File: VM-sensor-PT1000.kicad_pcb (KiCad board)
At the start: 2 copper layers, 26 x 24.8 mm, 20 parts, among them P1 PT100, P2 ADC, P3 PWR, U1 AMS1117, U2 MCP6001

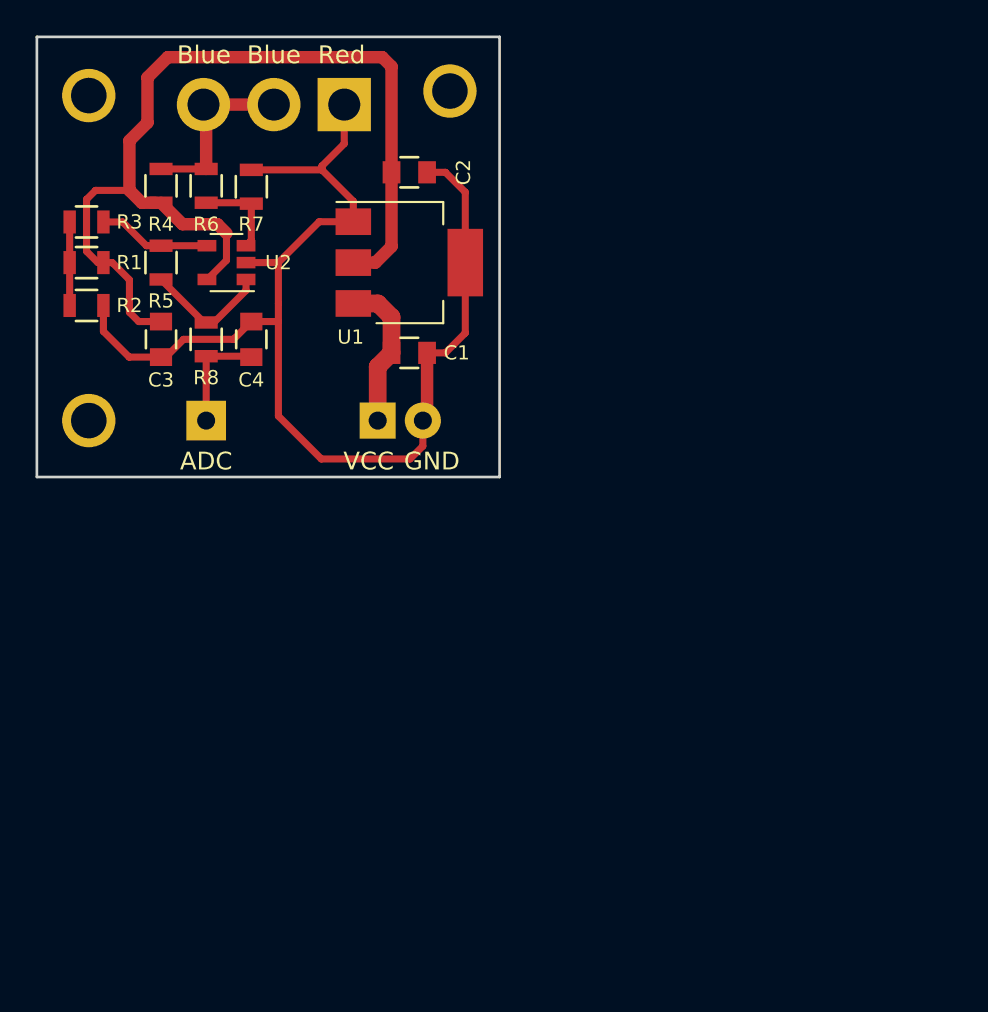
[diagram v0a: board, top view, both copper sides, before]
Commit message: add led PWR & change header ADC
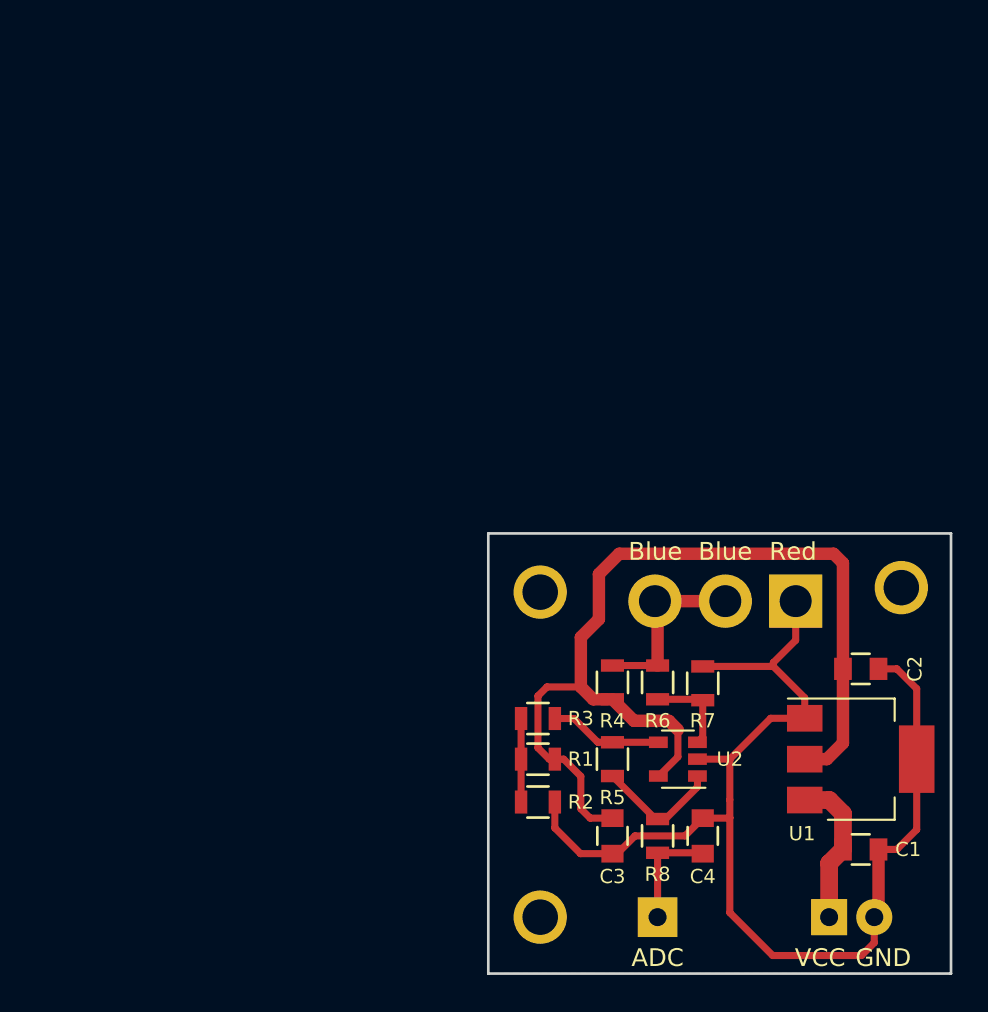
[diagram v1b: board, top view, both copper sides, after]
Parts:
- moved C1 37.8 mm to (160.0, 105.4)
- moved C2 37.8 mm to (160.0, 95.2)
- moved C3 37.8 mm to (146.1, 104.6)
- moved P1 37.8 mm to (156.4, 91.4)
- moved P2 37.8 mm to (148.6, 109.2)
- moved R1 37.8 mm to (141.9, 100.3)
- moved R2 37.8 mm to (141.9, 102.7)
- moved R3 37.8 mm to (141.9, 98.0)
- moved R4 37.8 mm to (146.1, 96.0)
- moved R5 37.8 mm to (146.1, 100.3)
- moved R6 37.8 mm to (148.6, 96.0)
- moved R8 37.8 mm to (148.6, 104.6)
- moved REF** 37.8 mm to (142.0, 90.9)
- moved REF** 37.8 mm to (162.3, 90.7)
- moved U1 37.8 mm to (160.0, 100.3)
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
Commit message: completed new PCB design
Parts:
- removed P1: PT100, Connectors_Hirose:Hirose_DF63-3P-3.96DSA_03x3.96mm_Straight
- removed REF** (x3): SolderWirePad_single_1-2mmDrill, Wire_Pads:SolderWirePad_single_1-2mmDrill
- added D1: LED_Small, LEDs:LED-3MM, F.Cu at (123.8, 89.2)
- added PT100: PT100, lib:Domino-PT100.pretty, F.Cu at (151.6, 96.2)
- added R9: 100R/1%, Resistors_SMD:R_0805, F.Cu at (127.5, 90.8)
- C3: value lib:C_0603 -> 10uF
- P2: footprint Pin_Headers:Pin_Header_Straight_1x01 -> w_conn_jst-ph:s2b-ph-kl
- P3: footprint Pin_Headers:Pin_Header_Straight_1x02 -> w_conn_jst-ph:s2b-ph-kl
- R2: value 100/1% -> 100R/1%
- R3, R6: value 1K/1% -> 16.9K/1%
- R5, R7: value 100K/1% -> 1M/1%
- U2: value MCP6001 -> MCP601T
- moved P3 40.1 mm to (126.4, 84.8), turned to 270 degrees
- moved U1 29.0 mm to (135.2, 85.4), turned to 180 degrees
- moved C1 28.7 mm to (141.9, 83.1)
- moved P2 25.7 mm to (126.4, 96.2)
- moved C4 22.3 mm to (130.9, 95.3)
- moved C2 20.6 mm to (141.9, 85.4)
- moved R8 17.8 mm to (133.4, 95.3)
- moved C3 17.4 mm to (141.9, 87.7), turned to 0 degrees
- moved R7 14.4 mm to (137.0, 98.8), turned to 180 degrees
- moved U2 13.7 mm to (137.0, 95.3), turned to 0 degrees
- moved R2 12.7 mm to (141.9, 90.0), turned to 180 degrees
- moved R5 12.2 mm to (137.0, 92.2), turned to 180 degrees
- moved R6 6.72 mm to (141.9, 96.6), turned to 0 degrees
- moved R1 5.93 mm to (141.9, 94.4), turned to 0 degrees
- moved R3 5.84 mm to (141.9, 92.2), turned to 0 degrees
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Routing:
- net GND: track 68.1 -> 110.0 mm
- net +3V3: track 55.9 -> 34.5 mm
- net /Blue: track 10.2 -> 18.2 mm
- net VCC: track 8.61 -> 15.8 mm
- net Net-(D1-Pad2): track 0.00 -> 4.12 mm
- net Net-(R6-Pad1): track 5.05 -> 7.79 mm
- net Net-(R5-Pad2): track 7.27 -> 4.76 mm
- net Net-(R3-Pad1): track 6.38 -> 7.95 mm
- net /ADC: track 6.18 -> 7.50 mm
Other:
- board size 26 x 24.8 mm -> 40 x 21 mm
- net class Default: trace_width 0.7 -> 1
- board text added: "+"
- board text added: "-"
- board text added: "BLUE"
- board text added: "PWR"
- board text added: "RED"
- board text removed: "ADC"
- board text removed: "Blue"
- board text removed: "GND"
- board text removed: "Red"
- board text removed: "VCC"
